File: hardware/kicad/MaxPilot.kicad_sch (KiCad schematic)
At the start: 12 parts, among them J1 Conn_01x03, U1 WeMos_D1_mini, U2 MOC3041M, U3 MOC3041M

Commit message: PCB v2.0: redesign for IPC-2221B/IEC 62368-1 mains safety compliance
- Replace J1 terminal block with 7.62mm pitch (was 5.08mm)
- Add IPC-2221B/IEC 62368-1 DRC rules (clearance ≥3.0mm mains↔LV,
  ≥2.5mm mains↔mains, creepage ≥5.0mm) in MaxPilot.kicad_dru
- Add MOC3041M_DIP6_W7.62mm_NC5 footprint: pin 5 (TRIAC substrate,
  DO NOT CONNECT) replaced with NPTH mechanical hole
- Assign mains nets to Line netclass (LINE, NEUT, LINE_P,
  Net-(D1-K), Net-(D2-A)); mains traces at 2mm width
- Re-route PCB to satisfy safety clearances (DRC: 0 errors)
- Update README: BOM, safety section, v2 changelog
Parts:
- J1: footprint TerminalBlock:TerminalBlock_bornier-3_P5.08mm -> MaxPilot:TerminalBlock_Generic_1x03_P7.62mm_Horizontal
- U2, U3: footprint Package_DIP:DIP-6_W7.62mm -> MaxPilot:MOC3041M_DIP6_W7.62mm_NC5
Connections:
- net LINE: no longer F1.2, PS1.1 (AC/L), RV1.1, U2.4, U3.4
- new net LINE_P: F1.2, PS1.1 (AC/L), RV1.1, U2.4, U3.4
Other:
- moved on the sheet: U1
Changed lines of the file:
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@@
+	(wire
+		(pts
+			(xy 130.81 76.2) (xy 130.81 78.74)
+		)
+		(stroke
+			(width 0)
+			(type default)
+		)
+	)
+	(wire
+		(pts
+			(xy 128.27 78.74) (xy 128.27 80.01)
+		)
+		(stroke
+			(width 0)
+			(type default)
+		)
+	)
+	(wire
+		(pts
+			(xy 130.81 78.74) (xy 128.27 78.74)
+		)
+		(stroke
+			(width 0)
+			(type default)
+		)
+	)
 	(wire
 		(pts
@@
 	(wire
 		(pts
+			(xy 128.27 36.83) (xy 125.73 36.83)
+		)
+		(stroke
+			(width 0)
+			(type default)
+		)
+	)
+	(wire
+		(pts
 			(xy 154.94 30.48) (xy 154.94 31.75)
 		)
@@
 	(wire
 		(pts
-			(xy 148.59 54.61) (xy 148.59 44.45)
+			(xy 148.59 53.34) (xy 148.59 44.45)
 		)
 		(stroke
@@
 	(wire
 		(pts
+			(xy 128.27 35.56) (xy 128.27 36.83)
+		)
+		(stroke
+			(width 0)
+			(type default)
+		)
+	)
+	(wire
+		(pts
 			(xy 189.23 53.34) (xy 189.23 67.31)
 		)
@@
 	(wire
 		(pts
-			(xy 138.43 54.61) (xy 148.59 54.61)
+			(xy 140.97 53.34) (xy 148.59 53.34)
 		)
 		(stroke
@@
 	(wire
 		(pts
-			(xy 149.86 64.77) (xy 149.86 72.39)
-		)
-		(stroke
-			(width 0)
-			(type default)
-		)
-	)
-	(wire
-		(pts
-			(xy 138.43 64.77) (xy 149.86 64.77)
+			(xy 149.86 63.5) (xy 149.86 72.39)
+		)
+		(stroke
+			(width 0)
+			(type default)
+		)
+	)
+	(wire
+		(pts
+			(xy 140.97 63.5) (xy 149.86 63.5)
 		)
 		(stroke
@@
 			)
 		)
-		(property "Footprint" "Package_DIP:DIP-6_W7.62mm"
+		(property "Footprint" "MaxPilot:MOC3041M_DIP6_W7.62mm_NC5"
 			(at 161.29 46.99 0)
 			(effects
@@
 			)
 		)
-		(property "Footprint" "Package_DIP:DIP-6_W7.62mm"
+		(property "Footprint" "MaxPilot:MOC3041M_DIP6_W7.62mm_NC5"
 			(at 161.29 74.93 0)
 			(effects
@@
 			)
 		)
-		(property "Value" "LINE"
+		(property "Value" "LINE_P"
 			(at 177.8 44.4499 90)
 			(effects
@@
 			)
 		)
-		(property "Value" "LINE"
+		(property "Value" "LINE_P"
 			(at 85.09 45.72 0)
 			(effects
@@
 			)
 		)
-		(property "Value" "LINE"
-			(at 66.04 44.45 0)
-			(effects
-				(font
-					(size 1.27 1.27)
-				)
+		(property "Value" "LINE_P"
+			(at 68.58 48.2599 0)
+			(effects
+				(font
+					(size 1.27 1.27)
+				)
+				(justify left)
 			)
 		)
@@
 	(symbol
 		(lib_id "MCU_Module:WeMos_D1_mini")
-		(at 128.27 57.15 0)
+		(at 130.81 55.88 0)
 		(unit 1)
 		(exclude_from_sim no)
@@
 		(fields_autoplaced yes)
 		(property "Reference" "U1"
-			(at 130.2894 77.47 0)
+			(at 132.8294 76.2 0)
 			(effects
 				(font
@@
 		)
 		(property "Value" "WeMos_D1_mini"
-			(at 130.2894 80.01 0)
+			(at 132.8294 78.74 0)
 			(effects
 				(font
@@
 		)
 		(property "Footprint" "Module:WEMOS_D1_mini_light"
-			(at 128.27 86.36 0)
+			(at 130.81 85.09 0)
 			(effects
 				(font
@@
 		)
 		(property "Datasheet" "https://wiki.wemos.cc/products:d1:d1_mini#documentation"
-			(at 81.28 86.36 0)
-			(effects
-				(font
-					(size 1.27 1.27)
-				)
-				(hide yes)
-			)
-		)
-		(property "Description" ""
-			(at 128.27 57.15 0)
+			(at 83.82 85.09 0)
+			(effects
+				(font
+					(size 1.27 1.27)
+				)
+				(hide yes)
+			)
+		)
+		(property "Description" ""
+			(at 130.81 55.88 0)
 			(effects
 				(font
@@
 			)
 		)
-		(property "Value" "LINE"
+		(property "Value" "LINE_P"
 			(at 78.74 38.354 0)
 			(effects
@@
 	(symbol
 		(lib_id "power:GND")
-		(at 128.27 77.47 0)
+		(at 128.27 80.01 0)
 		(unit 1)
 		(exclude_from_sim no)
@@
 		(fields_autoplaced yes)
 		(property "Reference" "#PWR0111"
-			(at 128.27 83.82 0)
+			(at 128.27 86.36 0)
 			(effects
 				(font
@@
 		)
 		(property "Value" "GND"
-			(at 128.27 82.55 0)
+			(at 128.27 85.09 0)
 			(effects
 				(font
@@
 		)
 		(property "Footprint" ""
-			(at 128.27 77.47 0)
+			(at 128.27 80.01 0)
 			(effects
 				(font
@@
 		)
 		(property "Datasheet" ""
-			(at 128.27 77.47 0)
-			(effects
-				(font
-					(size 1.27 1.27)
-				)
-				(hide yes)
-			)
-		)
-		(property "Description" ""
-			(at 128.27 77.47 0)
+			(at 128.27 80.01 0)
+			(effects
+				(font
+					(size 1.27 1.27)
+				)
+				(hide yes)
+			)
+		)
+		(property "Description" ""
+			(at 128.27 80.01 0)
 			(effects
 				(font
@@
 			)
 		)
-		(property "Value" "LINE"
+		(property "Value" "LINE_P"
 			(at 177.292 70.104 0)
 			(effects
@@
 			)
 		)
-		(property "Footprint" "TerminalBlock:TerminalBlock_bornier-3_P5.08mm"
+		(property "Footprint" "MaxPilot:TerminalBlock_Generic_1x03_P7.62mm_Horizontal"
 			(at 54.61 66.04 0)
 			(effects

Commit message: Add M2 mounting holes, reroute PCB, add 3D printable enclosure
- Add 4× M2 mounting holes at corners (H1-H4, annotated)
- Reroute PCB after component repositioning; DRC clean (9 warnings, 0 errors)
- Add hardware/enclosure/MaxPilot_box.scad: OpenSCAD parametric enclosure
  - Base with 4× M2 boss standoffs, friction-fit lid, J1 wire entry cutout
  - Box exterior ~107 × 46 × 36.6 mm, assembly with 4× M2×6 self-tapping screws
- Regenerate Gerbers and PCB images for updated layout
- Switch drill output to single unified .drl file
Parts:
- F1: footprint Fuse:Fuseholder_Blade_Mini_Keystone_3568 -> Resistor_THT:R_Axial_DIN0411_L9.9mm_D3.6mm_P15.24mm_Horizontal
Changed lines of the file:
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@@
 			)
 		)
-		(property "Footprint" "Fuse:Fuseholder_Blade_Mini_Keystone_3568"
+		(property "Footprint" "Resistor_THT:R_Axial_DIN0411_L9.9mm_D3.6mm_P15.24mm_Horizontal"
 			(at 73.66 41.91 0)
 			(effects

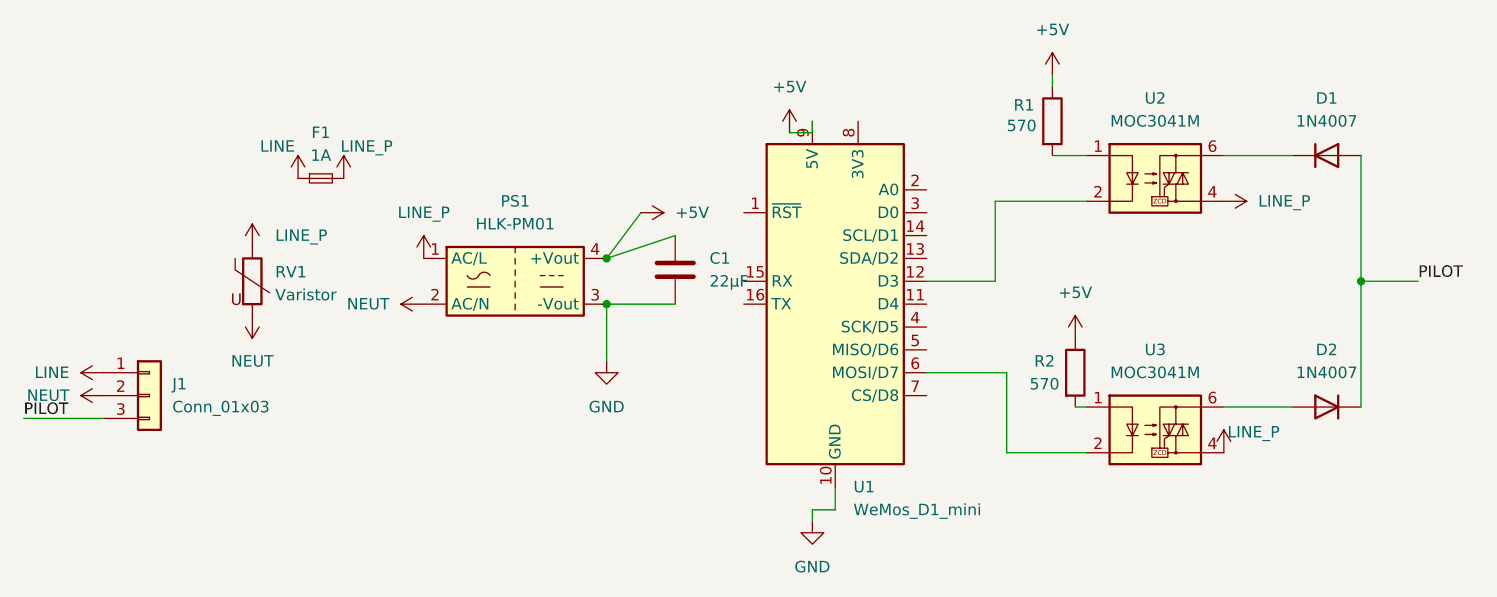
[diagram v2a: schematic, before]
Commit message: Improve schematic readability
- Fix 2 diagonal wires in PS1 DC output area (now orthogonal: vertical
  down from +5V symbol then horizontal to C1 top pin)
- Move +5V power symbol to standard orientation (rot=0, directly above
  PS1 +Vout pin)
- Add bold section labels: Entrée AC, Alim. 5V DC, MCU, Canal 1 (SSR1),
  Canal 2 (SSR2)
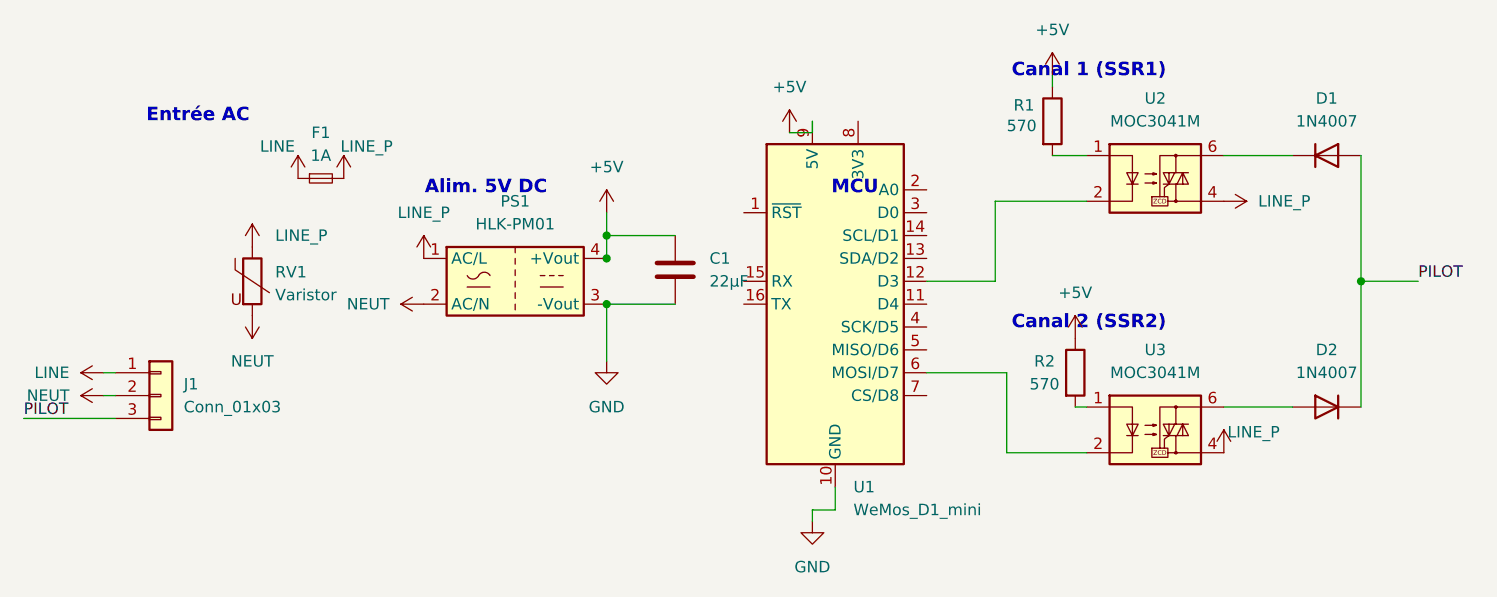
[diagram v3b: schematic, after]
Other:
- note added: "Alim. 5V DC"
- note added: "Canal 1 (SSR1)"
- note added: "Canal 2 (SSR2)"
- note added: "Entrée AC"
- note added: "MCU"
- title: (none) -> MaxPilot
- moved on the sheet: J1
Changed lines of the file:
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@@
 	(generator_version "9.0")
 	(paper "A4")
+	(title_block
+		(title "MaxPilot")
+		(rev "2.0")
+		(comment 1 "CERN Open Hardware Licence Version 2 ")
+	)
 	(junction
 		(at 105.41 50.8)
@@
 	(wire
 		(pts
-			(xy 109.22 45.72) (xy 105.41 50.8)
-		)
-		(stroke
-			(width 0)
-			(type default)
-		)
-	)
-	(wire
-		(pts
 			(xy 128.27 36.83) (xy 125.73 36.83)
 		)
@@
 	(wire
 		(pts
+			(xy 50.8 66.04) (xy 49.53 66.04)
+		)
+		(stroke
+			(width 0)
+			(type default)
+		)
+	)
+	(wire
+		(pts
 			(xy 189.23 39.37) (xy 189.23 53.34)
 		)
@@
 	(wire
 		(pts
+			(xy 50.8 63.5) (xy 49.53 63.5)
+		)
+		(stroke
+			(width 0)
+			(type default)
+		)
+	)
+	(wire
+		(pts
 			(xy 149.86 72.39) (xy 158.75 72.39)
 		)
@@
 	(wire
 		(pts
-			(xy 105.41 50.8) (xy 113.03 48.26)
-		)
-		(stroke
-			(width 0)
-			(type default)
-		)
-	)
-	(wire
-		(pts
 			(xy 173.99 39.37) (xy 181.61 39.37)
 		)
@@
 	(wire
 		(pts
-			(xy 40.64 68.58) (xy 49.53 68.58)
-		)
-		(stroke
-			(width 0)
-			(type default)
+			(xy 40.64 68.58) (xy 50.8 68.58)
+		)
+		(stroke
+			(width 0)
+			(type default)
+		)
+	)
+	(wire
+		(pts
+			(xy 105.41 45.72) (xy 105.41 50.8)
+		)
+		(stroke
+			(width 0)
+			(type default)
+		)
+	)
+	(wire
+		(pts
+			(xy 105.41 48.26) (xy 113.03 48.26)
+		)
+		(stroke
+			(width 0)
+			(type default)
+		)
+	)
+	(junction
+		(at 105.41 48.26)
+		(diameter 0)
+		(color 0 0 0 0)
+	)
+	(text "Entrée AC"
+		(at 60 35 0)
+		(effects
+			(font
+				(size 1.5 1.5)
+				(bold yes)
+			)
+		)
+	)
+	(text "Alim. 5V DC"
+		(at 92 43 0)
+		(effects
+			(font
+				(size 1.5 1.5)
+				(bold yes)
+			)
+		)
+	)
+	(text "MCU"
+		(at 133 43 0)
+		(effects
+			(font
+				(size 1.5 1.5)
+				(bold yes)
+			)
+		)
+	)
+	(text "Canal 1 (SSR1)"
+		(at 159 30 0)
+		(effects
+			(font
+				(size 1.5 1.5)
+				(bold yes)
+			)
+		)
+	)
+	(text "Canal 2 (SSR2)"
+		(at 159 58 0)
+		(effects
+			(font
+				(size 1.5 1.5)
+				(bold yes)
+			)
 		)
 	)
@@
 	(symbol
 		(lib_id "power:+5V")
-		(at 109.22 45.72 270)
+		(at 105.41 45.72 0)
 		(unit 1)
 		(exclude_from_sim no)
@@
 		(fields_autoplaced yes)
 		(property "Reference" "#PWR0108"
+			(at 105.41 49.53 0)
+			(effects
+				(font
+					(size 1.27 1.27)
+				)
+				(hide yes)
+			)
+		)
+		(property "Value" "+5V"
+			(at 105.41 40.64 0)
+			(effects
+				(font
+					(size 1.27 1.27)
+				)
+			)
+		)
+		(property "Footprint" ""
 			(at 105.41 45.72 0)
 			(effects
@@
 			)
 		)
-		(property "Value" "+5V"
-			(at 113.03 45.7199 90)
-			(effects
-				(font
-					(size 1.27 1.27)
-				)
-				(justify left)
-			)
-		)
-		(property "Footprint" ""
-			(at 109.22 45.72 0)
-			(effects
-				(font
-					(size 1.27 1.27)
-				)
-				(hide yes)
-			)
-		)
 		(property "Datasheet" ""
-			(at 109.22 45.72 0)
-			(effects
-				(font
-					(size 1.27 1.27)
-				)
-				(hide yes)
-			)
-		)
-		(property "Description" ""
-			(at 109.22 45.72 0)
+			(at 105.41 45.72 0)
+			(effects
+				(font
+					(size 1.27 1.27)
+				)
+				(hide yes)
+			)
+		)
+		(property "Description" ""
+			(at 105.41 45.72 0)
 			(effects
 				(font
@@
 	(symbol
 		(lib_id "Connector_Generic:Conn_01x03")
-		(at 54.61 66.04 0)
+		(at 55.88 66.04 0)
 		(unit 1)
 		(exclude_from_sim no)
@@
 		(fields_autoplaced yes)
 		(property "Reference" "J1"
-			(at 57.15 64.7699 0)
+			(at 58.42 64.7699 0)
 			(effects
 				(font
@@
 		)
 		(property "Value" "Conn_01x03"
-			(at 57.15 67.3099 0)
+			(at 58.42 67.3099 0)
 			(effects
 				(font
@@
 		)
 		(property "Footprint" "MaxPilot:TerminalBlock_Generic_1x03_P7.62mm_Horizontal"
-			(at 54.61 66.04 0)
+			(at 55.88 66.04 0)
 			(effects
 				(font
@@
 		)
 		(property "Datasheet" "~"
-			(at 54.61 66.04 0)
-			(effects
-				(font
-					(size 1.27 1.27)
-				)
-				(hide yes)
-			)
-		)
-		(property "Description" ""
-			(at 54.61 66.04 0)
-			(effects
-				(font
+			(at 55.88 66.04 0)
+			(effects
+				(font
+					(size 1.27 1.27)
+				)
+				(hide yes)
+			)
+		)
+		(property "Description" ""
+			(at 55.88 66.04 0)
+			(effects
+				(font
